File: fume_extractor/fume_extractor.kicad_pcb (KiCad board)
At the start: 4 copper layers, 18 parts, among them J1 Conn_01x04_MountingPin, J2 USB_C_Receptacle_USB2.0_16P, Q1 Q_NPN_BCE, U1 ATtiny1626-M

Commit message: rev 1
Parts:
- removed Q1: Q_NPN_BCE, Package_TO_SOT_SMD:SOT-223-3_TabPin2
- removed TP1, TP2, TP3, TP4, TP5, TP6: TestPoint, TestPoint:TestPoint_THTPad_D1.0mm_Drill0.5mm
- added C2: 4.7 uF, Capacitor_SMD:C_0603_1608Metric, F.Cu at (80.0, 48.8)
- added C3: 10 pF, Capacitor_SMD:C_0603_1608Metric, F.Cu at (75.8, 53.4)
- added C4: 1 uF, Capacitor_SMD:C_0603_1608Metric, F.Cu at (78.0, 57.0)
- added D1: D, Diode_SMD:D_SOD-123, F.Cu at (80.8, 55.4)
- added J3: Conn_01x04, Connector_PinHeader_2.54mm:PinHeader_1x04_P2.54mm_Vertical, F.Cu at (87.0, 63.8)
- added L1: 10 uH, unsurv_offline_pcb_footprints:CR32, F.Cu at (84.2, 51.8)
- added U2: TPS61040DRV, Package_SON:WSON-6-1EP_2x2mm_P0.65mm_EP1x1.6mm, F.Cu at (80.0, 51.5)
- added U3: ~, unsurv_offline_pcb_footprints:testpoint_array_2x3, B.Cu at (70.0, 46.5)
- J1: value Conn_01x04_MountingPin -> Conn_01x04
- R1: value 2.2k -> 100k
- R2: value 4.7k -> 866k
- moved J1 99.7 mm to (66.2, 43.0), turned to 90 degrees
- moved R6 98.5 mm to (60.2, 61.5)
- moved R5 98.5 mm to (60.2, 59.0)
- moved J2 96.2 mm to (53.4, 60.0), turned to -90 degrees
- moved U1 92.0 mm to (70.0, 60.0), turned to 135 degrees
- moved R1 83.8 mm to (77.4, 50.2), turned to -90 degrees
- moved R2 83.4 mm to (77.4, 53.4), turned to -90 degrees
- moved C1 79.6 mm to (72.6, 62.6), turned to -135 degrees
- moved R4 79.2 mm to (79.2, 63.0), turned to 180 degrees
- moved R3 76.6 mm to (79.2, 65.0)
- moved POT1 66.8 mm to (73.8, 69.4), turned to 180 degrees
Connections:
- C1 pad 1: VCC -> +5V
- J1 pad 1: unconnected-(J1-Pin_1-Pad1) -> +5V
- J1 pad 2: unconnected-(J1-Pin_2-Pad2) -> SDA
- J1 pad 3: unconnected-(J1-Pin_3-Pad3) -> SCL
- J1 pad 4: unconnected-(J1-Pin_4-Pad4) -> GND
- J2 pad A4: VCC -> +5V
- J2 pad A9: VCC -> +5V
- J2 pad B4: VCC -> +5V
- J2 pad B9: VCC -> +5V
- POT1 pad 1: VCC -> +5V
- R1 pad 1: +12V -> GND
- R1 pad 2: FAN_PWM -> Net-(U2-FB)
- R2 pad 1: Net-(R2-Pad1) -> Net-(U2-FB)
- R2 pad 2: Net-(Q1-B) -> +12V
- R3 pad 2: Net-(R2-Pad1) -> FAN_PWM
- R4 pad 1: Net-(R2-Pad1) -> FAN_PWM
- U1 pad 1: unconnected-(U1-PA2-Pad1) -> SDA
- U1 pad 13: SDA -> unconnected-(U1-PB1-Pad13)
- U1 pad 14: SCL -> unconnected-(U1-PB0-Pad14)
- U1 pad 2: unconnected-(U1-PA3-Pad2) -> SCL
- U1 pad 4: VCC -> +5V
- U1 pad 7: unconnected-(U1-PA6-Pad7) -> FAN_RPM
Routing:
- net SCL: track 0.00 -> 22.5 mm, vias 0 -> 1
- net SDA: track 0.00 -> 22.1 mm, vias 0 -> 1
- net UPDI: track 0.00 -> 18.9 mm, vias 0 -> 2
- net unconnected-(J2-SHIELD-PadS1): track 0.00 -> 18.1 mm
- net FAN_RPM: track 0.00 -> 17.6 mm, vias 0 -> 1
- net TX: track 0.00 -> 15.1 mm, vias 0 -> 1
- net +5V: track 0.00 -> 13.1 mm, vias 0 -> 8
- net Net-(J2-GND-PadA1): track 0.00 -> 12.5 mm
- net RX: track 0.00 -> 11.9 mm, vias 0 -> 1
- net PWM1: track 0.00 -> 9.07 mm, vias 0 -> 2
- net FAN_PWM: track 0.00 -> 9.05 mm
- net PWM: track 0.00 -> 8.75 mm, vias 0 -> 2
- net +12V: track 0.00 -> 6.90 mm
- net GND: track 0.00 -> 6.48 mm, vias 0 -> 3
- net Net-(U2-FB): track 0.00 -> 5.24 mm
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- added copper zone on F.Cu, net +12V
- added copper zone on F.Cu, net +5V
- added copper zone on In1.Cu, net +5V
- added copper zone on B.Cu, net GND
- added copper zone on F.Cu, net GND
- added copper zone on In2.Cu, net GND
- added copper zone on F.Cu, net Net-(D1-A)
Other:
- board outline added: 40 x 40 mm

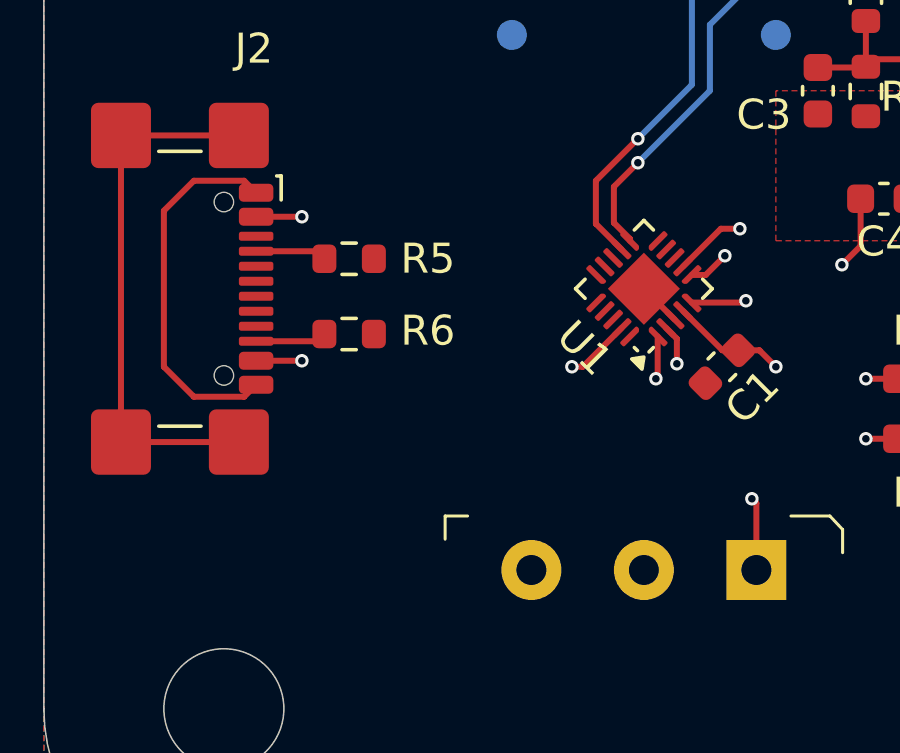
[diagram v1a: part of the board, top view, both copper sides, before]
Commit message: fix GND connection on USB C
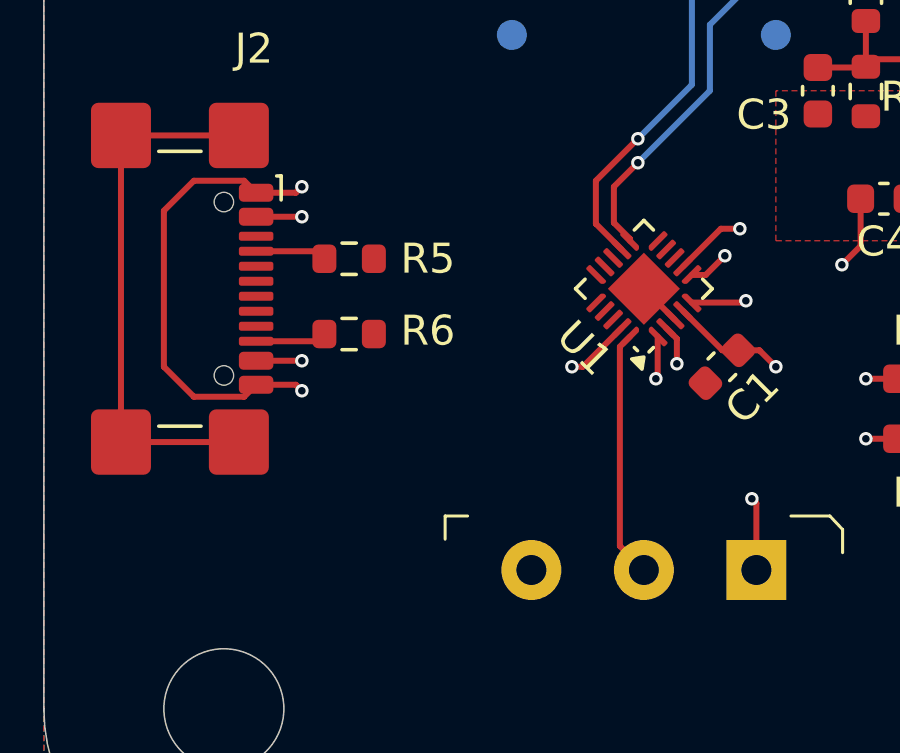
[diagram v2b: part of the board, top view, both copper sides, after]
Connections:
- J2 pad A1: Net-(J2-GND-PadA1) -> GND
- J2 pad A12: Net-(J2-GND-PadA1) -> GND
- J2 pad B1: Net-(J2-GND-PadA1) -> GND
- J2 pad B12: Net-(J2-GND-PadA1) -> GND
- U1 pad 20: unconnected-(U1-PA1-Pad20) -> ANALOG_READ
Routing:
- net GND: track 6.48 -> 22.2 mm, vias 3 -> 5
- net Net-(J2-GND-PadA1): track 12.5 -> 0.00 mm
- net ANALOG_READ: track 0.00 -> 8.26 mm
